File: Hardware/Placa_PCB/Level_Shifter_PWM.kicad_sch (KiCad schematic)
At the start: 3 parts, among them U2 TXU0104PWR

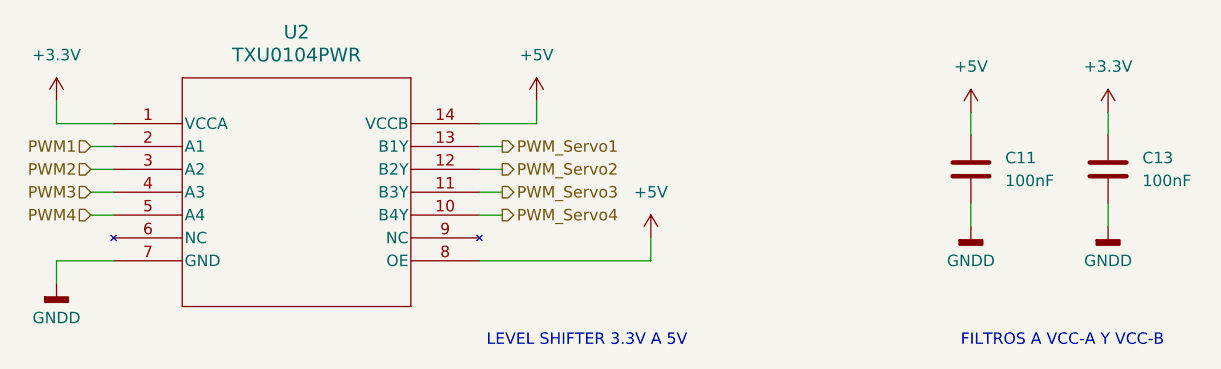
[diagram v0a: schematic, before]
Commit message: Agregando MCU al esquematico
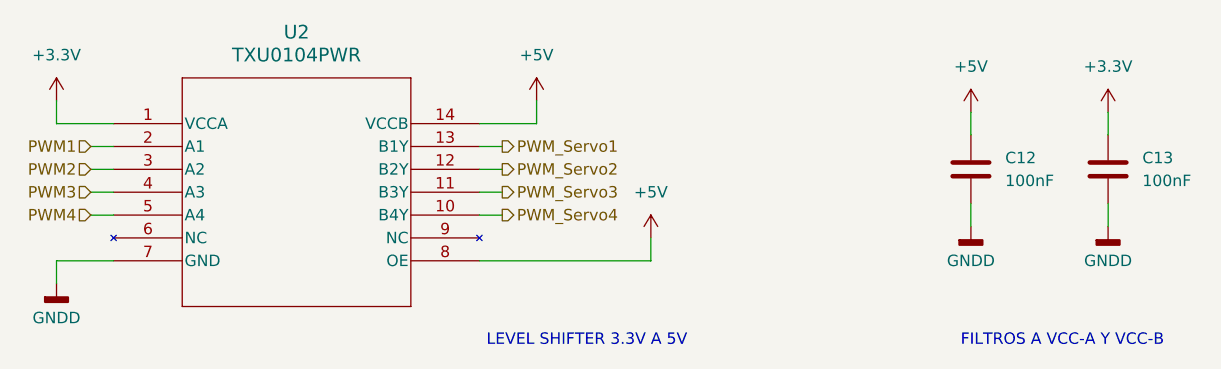
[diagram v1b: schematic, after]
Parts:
- renumbered C11 to C12
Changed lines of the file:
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@@
 		(dnp no)
 		(fields_autoplaced yes)
-		(property "Reference" "C11"
+		(property "Reference" "C12"
 			(at 190.5 87.6299 0)
 			(effects
@@
 			(project ""
 				(path "/ca162c4b-e7f6-494c-9ea1-0d86ef4a8e44/0655d80b-ec39-4060-bfcf-9e46930fb85c"
-					(reference "C11")
+					(reference "C12")
 					(unit 1)
 				)

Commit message: Esquematico Final
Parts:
- C12, C13: footprint (none) -> Capacitor_SMD:C_0805_2012Metric_Pad1.18x1.45mm_HandSolder
- renumbered U2 to U3
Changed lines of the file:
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@@
 		(dnp no)
 		(fields_autoplaced yes)
-		(property "Reference" "U2"
+		(property "Reference" "U3"
 			(at 111.76 73.66 0)
 			(effects
@@
 			(project ""
 				(path "/ca162c4b-e7f6-494c-9ea1-0d86ef4a8e44/0655d80b-ec39-4060-bfcf-9e46930fb85c"
-					(reference "U2")
+					(reference "U3")
 					(unit 1)
 				)
@@
 			)
 		)
-		(property "Footprint" ""
+		(property "Footprint" "Capacitor_SMD:C_0805_2012Metric_Pad1.18x1.45mm_HandSolder"
 			(at 187.6552 92.71 0)
 			(effects
@@
 			)
 		)
-		(property "Footprint" ""
+		(property "Footprint" "Capacitor_SMD:C_0805_2012Metric_Pad1.18x1.45mm_HandSolder"
 			(at 202.8952 92.71 0)
 			(effects
